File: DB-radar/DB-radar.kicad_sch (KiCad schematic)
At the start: 66 parts, among them J1 Conn_01x10_Female, J2 USB_C_Receptacle, Q1 FS8205A, Q1 PN2222A, SW1 SW_Push, SW2 SW_SPDT, SW4 SW_MEC_5G, U1 ATmega328PB-A, U2 DW01A-G, U3 TP4056, U4 XC6206PxxxMR, U5 4052, U6 4052, U7 4052, U8 4052, Y1 Crystal_GND3_Small

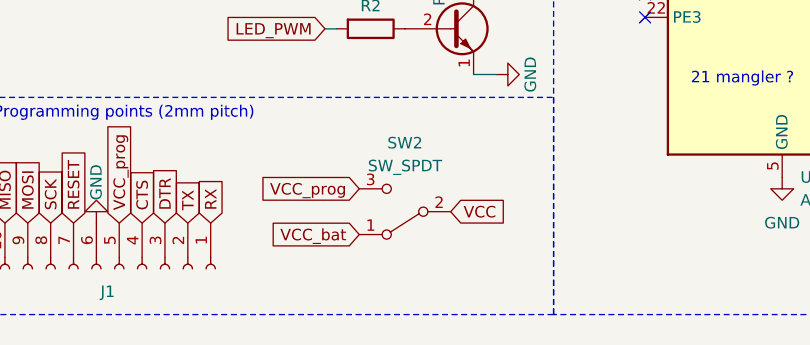
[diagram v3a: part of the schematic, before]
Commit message: Fulførte routing og passed DRC
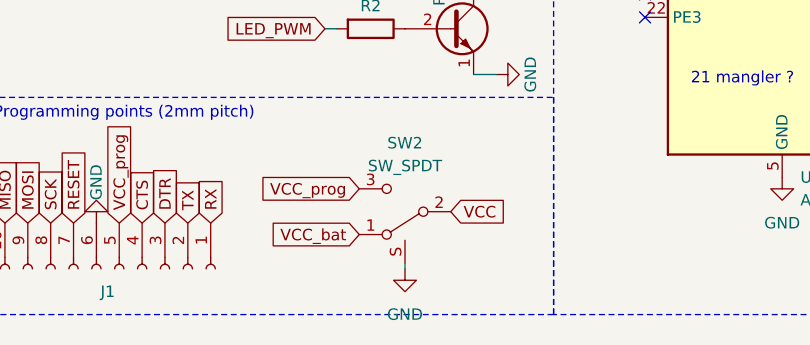
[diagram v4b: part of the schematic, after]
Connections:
- net GND: now also SW2.S (Shield)
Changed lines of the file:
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@@
+    (stroke (width 0) (type default))
+  )
+  (wire (pts (xy 59.69 193.675) (xy 59.69 194.31))
     (stroke (width 0) (type default))
   )
@@
         (path "/b1ef8062-d0b2-45f0-be8f-ceb4fd46a2d8"
           (reference "R1") (unit 1)
+        )
+      )
+    )
+  )
+  (symbol (lib_id "power:GND") (at 59.69 194.31 0) (unit 1)
+    (in_bom yes) (on_board yes) (dnp no) (fields_autoplaced)
+    (property "Reference" "#PWR025" (at 59.69 200.66 0)
+      (effects (font (size 1.27 1.27)) hide)
+    )
+    (property "Value" "GND" (at 59.69 199.39 0)
+      (effects (font (size 1.27 1.27)))
+    )
+    (property "Footprint" "" (at 59.69 194.31 0)
+      (effects (font (size 1.27 1.27)) hide)
+    )
+    (property "Datasheet" "" (at 59.69 194.31 0)
+      (effects (font (size 1.27 1.27)) hide)
+    )
+    (pin "1")
+    (instances
+      (project "DB-radar"
+        (path "/4fe367bb-912f-4df7-b060-07157080bb20"
+          (reference "#PWR025") (unit 1)
+        )
+      )
+      (project "fish clock"
+        (path "/8a39ddf7-266a-4e35-8762-e2f31a43cf6c"
+          (reference "#PWR0107") (unit 1)
         )
       )
@@
     (pin "2")
     (pin "3")
-    (instances
-      (project "DB-radar"
+    (pin "S")
+    (instances
+      (project "DB-radar"
